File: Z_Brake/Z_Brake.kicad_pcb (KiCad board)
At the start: 2 copper layers, 55.9 x 35.6 mm, 26 parts, among them K1 EC2-24NU, K2 EC2-24NU, P1 CONN_01X04, P2 CONN_01X02, P3 CONN_01X04, Q1 2N7002, U1 LM397

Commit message: Final PCB
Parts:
- added REF**: Symbol_GNU-GPL_CopperTop_Small, Symbol:Symbol_GNU-GPL_CopperTop_Small, B.Cu at (67.9, 116.8)
- added REF**: OSHW-Logo2_9.8x8mm_Copper, Symbol:OSHW-Logo2_9.8x8mm_Copper, B.Cu at (77.5, 116.2)
- moved MH4 12.3 mm to (99.7, 120.7)
- moved MH3 11.4 mm to (59.1, 120.7)
- moved RV1 7.22 mm to (91.4, 112.4)
- moved P3 7.01 mm to (88.9, 117.5)
- moved RV2 6.41 mm to (86.4, 112.4)
- moved MH2 5.85 mm to (99.7, 80.0)
- moved MH1 3.86 mm to (59.1, 80.0)
- moved D3 2.54 mm to (83.8, 104.8)
- moved K2 2.54 mm to (83.8, 96.5)
- moved R1 1.98 mm to (62.5, 97.8)
- moved R5 1.78 mm to (68.6, 95.8)
- moved R2 1.66 mm to (64.3, 102.5)
- moved R3 1.48 mm to (64.3, 97.8)
- moved D1 1.42 mm to (66.0, 90.8)
- moved P1 1.42 mm to (88.9, 83.2)
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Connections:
- D4 pad 1: VDD -> Net-(D4-Pad1)
- D4 pad 2: Net-(D4-Pad2) -> VDD
- R7 pad 1: Net-(D4-Pad2) -> Net-(D4-Pad1)
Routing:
- net GND: track 0.00 -> 221.6 mm, vias 0 -> 2
- net VDD: track 0.00 -> 72.8 mm
- net Net-(K2-Pad9): track 0.00 -> 32.9 mm
- net Net-(K1-Pad4): track 0.00 -> 32.9 mm
- net Net-(D2-Pad2): track 0.00 -> 31.5 mm
- net Net-(K2-Pad4): track 0.00 -> 31.3 mm
- net Net-(K1-Pad9): track 0.00 -> 31.3 mm
- net Net-(C1-Pad1): track 0.00 -> 16.3 mm
- net Net-(D1-Pad1): track 0.00 -> 14.4 mm
- net Net-(C1-Pad2): track 0.00 -> 13.9 mm
- net +24V: track 0.00 -> 11.5 mm
- net Net-(K1-Pad5): track 0.00 -> 9.15 mm
- net Net-(K2-Pad8): track 0.00 -> 9.07 mm
- net Net-(K2-Pad5): track 0.00 -> 8.02 mm
- net Net-(K1-Pad8): track 0.00 -> 8.02 mm
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- added copper zone on B.Cu, net GND
- added copper zone on F.Cu, net GND
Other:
- board size 55.9 x 35.6 mm -> 47 x 47 mm
- net class Default: trace_width 0.381 -> 0.25; via_dia 1.016 -> 1.2; via_drill 0.508 -> 0.6
- net class STD_Signal removed
- net class VDD added: clearance 0.2, trace_width 1, via_dia 1.6, via_drill 0.8
- rule via_min_drill: 0.508 -> 0.4
- rule via_min_size: 1.016 -> 0.8
- board text added: "24V"
- board text added: "A"
- board text added: "A/"
- board text added: "B"
- board text added: "B/"
- board text added: "GND"
- board text added: "Original 2 motor design by Aleph Objects 2018"
- board text added: "Project R3D / Adam Haile"
- board text added: "Z Motor Brake"
- board text added: "v1.0.0"
- board text added: "© 2021"
- board text removed: "Aleph Objects"
- board text removed: "GPLv3"
- board text removed: "Motor Brake"
- board text removed: "PC-BD0096"
- board text removed: "REV. C"
- board text removed: "© 2018"

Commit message: Add fab files
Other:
- board text removed: "Original 2 motor design by Aleph Objects 2018"

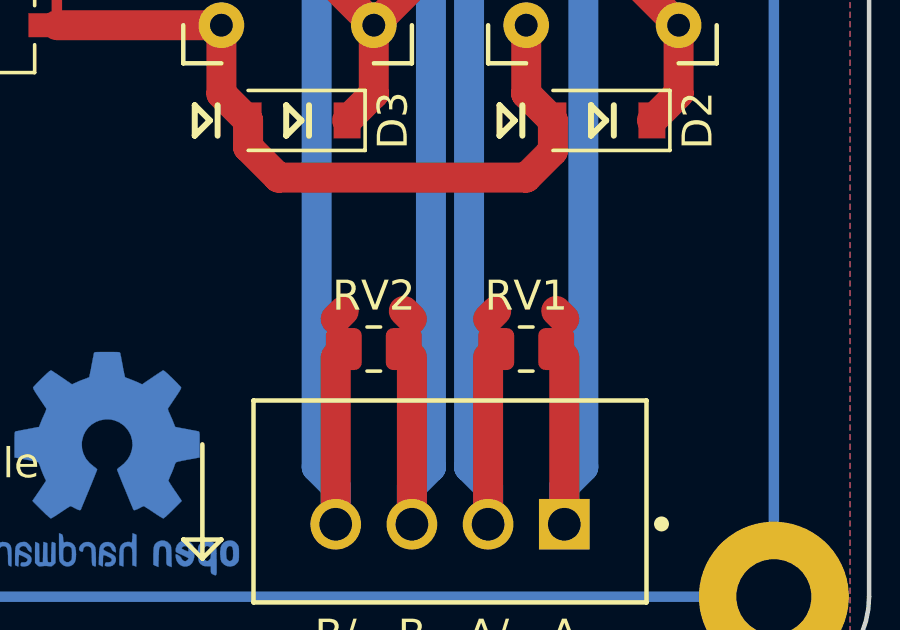
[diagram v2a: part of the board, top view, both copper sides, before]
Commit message: Added smt relay version
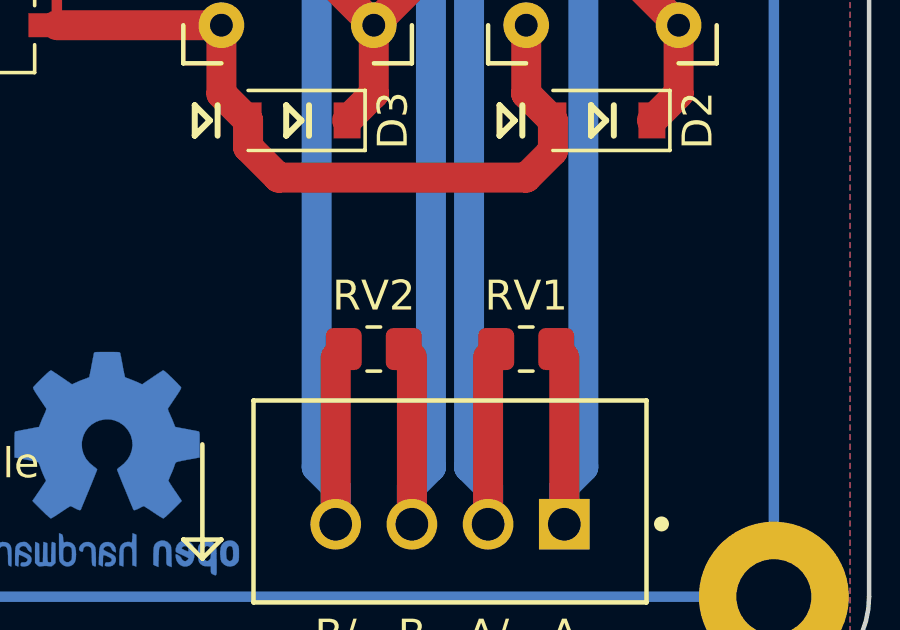
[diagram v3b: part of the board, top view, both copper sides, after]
